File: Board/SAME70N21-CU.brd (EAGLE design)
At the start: 53.3 x 40.3 mm, 35 parts, among them U1 ATSAME70N21A-ANTQFP100_14X14M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

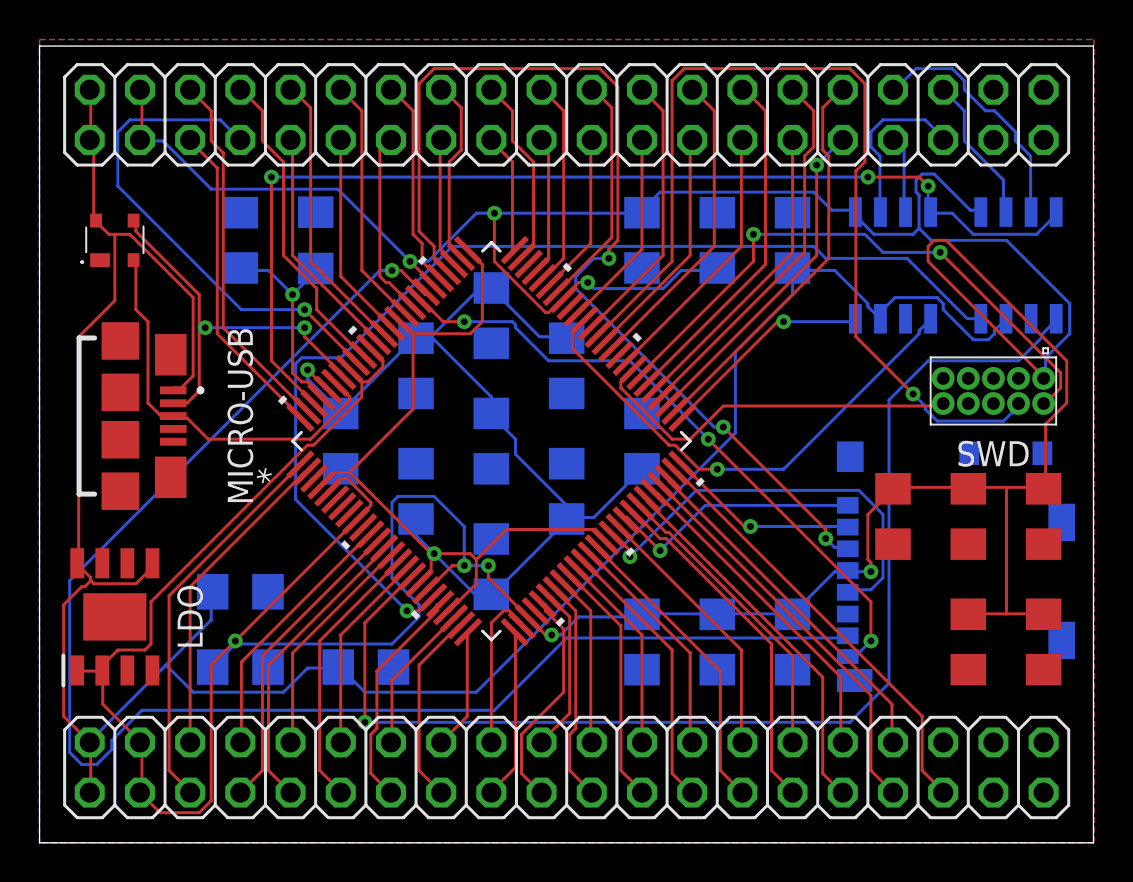
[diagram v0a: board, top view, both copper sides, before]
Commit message: Major revision to first board pcb
- reduced board size
- fixed airwires
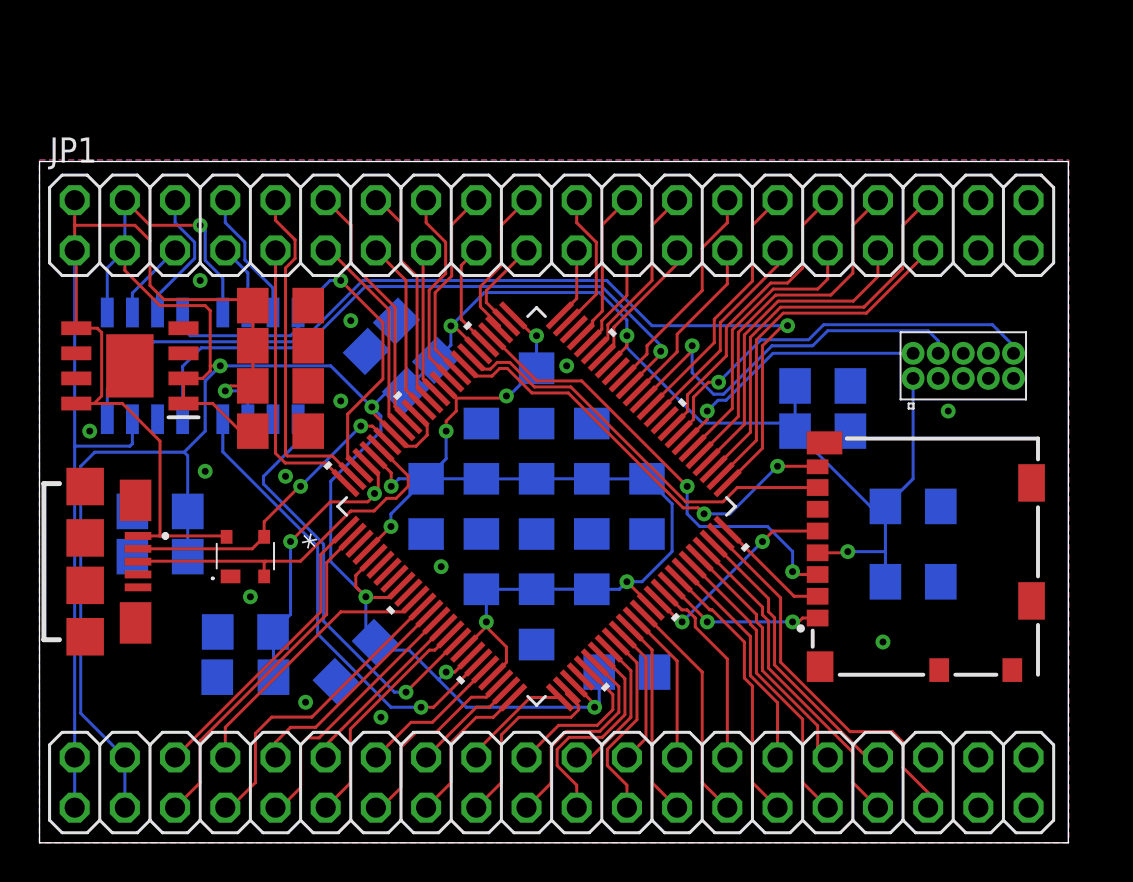
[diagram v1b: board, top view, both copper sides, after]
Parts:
- removed JP3: (no value), pinhead:2X20
- added JP1: (no value), pinhead:2X20
- moved C1 44.9 mm to (6.10, 14.5), flipped to the bottom, turned to 0 degrees
- moved C20 40.9 mm to (6.10, 16.8), flipped to the bottom, turned to 0 degrees
- moved CAN0 38.7 mm to (11.2, 24.1)
- moved CAN1 38.2 mm to (5.33, 24.1)
- moved C2 31.0 mm to (16.0, 9.14), flipped to the bottom, turned to 315 degrees
- moved C21 26.5 mm to (12.2, 25.1), flipped to the top, turned to 0 degrees
- moved C6 24.4 mm to (19.1, 25.4), turned to 45 degrees
- moved C3 22.5 mm to (29.7, 8.64), flipped to the bottom, turned to 180 degrees
- moved R1 22.4 mm to (10.4, 8.38), turned to 180 degrees
- moved C19 19.8 mm to (10.4, 10.7), turned to 0 degrees
- moved C8 18.9 mm to (17.5, 23.9), turned to 45 degrees
- moved ESD 17.3 mm to (10.4, 14.5)
- moved C22 14.9 mm to (12.2, 23.1), flipped to the top, turned to 0 degrees
- moved C23 14.6 mm to (12.2, 27.2), flipped to the top, turned to 0 degrees
- moved C5 13.3 mm to (39.6, 20.8), turned to 180 degrees
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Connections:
- net +3V3: now also JP1.3, JP1.4; no longer JP3.3, JP3.4
- net +5V: now also JP1.1, JP1.2; no longer JP3.1, JP3.2
- net ATSAME70N21_PA0: now also JP1.24; no longer JP3.19
- net ATSAME70N21_PA1: now also JP1.26; no longer JP3.21
- net ATSAME70N21_PA13: now also JP2.17; no longer JP2.18
- net ATSAME70N21_PA16: now also JP2.20; no longer JP2.19
- net ATSAME70N21_PA17: now also JP2.11; no longer JP2.12
- net ATSAME70N21_PA18: now also JP2.12; no longer JP2.11
- net ATSAME70N21_PA19: now also JP2.9; no longer JP2.10
- net ATSAME70N21_PA2: now also JP1.28; no longer JP3.23
- net ATSAME70N21_PA20: now also JP2.10; no longer JP2.9
- net ATSAME70N21_PA21: now also JP2.14; no longer JP2.13
- net ATSAME70N21_PA22: now also JP2.18; no longer JP2.17
- net ATSAME70N21_PA23: now also JP2.19; no longer JP2.20
- net ATSAME70N21_PA3: now also JP1.27; no longer JP3.24
- net ATSAME70N21_PA4: now also JP1.34; no longer JP3.29
- net ATSAME70N21_PA5: now also JP1.35; no longer JP3.32
- net ATSAME70N21_PA7: now also JP2.16; no longer JP2.15
- net ATSAME70N21_PA8: now also JP2.15; no longer JP2.16
- net ATSAME70N21_PA9: now also JP1.33; no longer JP3.30
- net ATSAME70N21_PB12: now also JP1.29; no longer JP3.26
- net ATSAME70N21_PB13: now also JP1.9; no longer JP3.5
- net ATSAME70N21_PB4: now also JP1.22; no longer JP3.18
- net ATSAME70N21_PB5: now also JP1.19; no longer JP3.16
- net ATSAME70N21_PB9: now also JP1.10; no longer JP3.6
- net ATSAME70N21_PD0: now also JP2.6; no longer JP2.5
- net ATSAME70N21_PD1: now also JP1.11; no longer JP3.7
- net ATSAME70N21_PD10: now also JP1.23; no longer JP3.20
- net ATSAME70N21_PD11: now also JP1.25; no longer JP3.22
- net ATSAME70N21_PD13: now also JP1.30; no longer JP3.25
- net ATSAME70N21_PD14: now also JP1.32; no longer JP3.27
- net ATSAME70N21_PD15: now also JP1.21; no longer JP3.17
- net ATSAME70N21_PD16: now also JP1.31; no longer JP3.28
- net ATSAME70N21_PD17: now also JP1.36; no longer JP3.31
- net ATSAME70N21_PD2: now also JP1.12; no longer JP3.8
- net ATSAME70N21_PD3: now also JP1.13; no longer JP3.9
- net ATSAME70N21_PD30: now also JP2.13; no longer JP2.14
- net ATSAME70N21_PD31: now also JP2.5; no longer JP2.6
- net ATSAME70N21_PD4: now also JP1.14; no longer JP3.10
- net ATSAME70N21_PD5: now also JP1.15; no longer JP3.11
- net ATSAME70N21_PD6: now also JP1.16; no longer JP3.12
- net ATSAME70N21_PD7: now also JP1.18; no longer JP3.13
- net ATSAME70N21_PD8: now also JP1.17; no longer JP3.14
- net ATSAME70N21_PD9: now also JP1.20; no longer JP3.15
- net CAN0H: now also JP1.8; no longer JP3.34
- net CAN0L: now also JP1.7; no longer JP3.36
- net CAN1H: now also JP1.6; no longer JP3.33
- net CAN1L: now also JP1.5; no longer JP3.35
- net GND: now also JP1.37, JP1.38, JP1.39, JP1.40; no longer JP3.37, JP3.38, JP3.39, JP3.40
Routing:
- net +3V3: track 243.3 -> 171.3 mm, vias 8 -> 9
- net MSD-DAT0: track 76.4 -> 21.1 mm, vias 1 -> 0
- net +5V: track 122.9 -> 79.3 mm, vias 0 -> 1
- net CAN0TX: track 60.3 -> 21.5 mm
- net CAN1RX: track 10.8 -> 48.6 mm
- net CAN-STBY: track 54.6 -> 22.0 mm, vias 3 -> 1
- net CAN0RX: track 55.1 -> 23.5 mm
- net VCCINT: track 88.1 -> 56.8 mm, vias 2 -> 7
- net MSD-CMD: track 51.9 -> 22.9 mm, vias 3 -> 2
- net SWCLK: track 48.2 -> 20.2 mm
- net SWDIO: track 29.9 -> 13.6 mm, vias 2 -> 1
- net ATSAME70N21_PD1: track 25.4 -> 10.6 mm, vias 1 -> 0
- net MSD-CLK: track 21.5 -> 10.5 mm, vias 1 -> 2
- net MSD-DAT1: track 32.8 -> 22.4 mm, vias 3 -> 2
- net CAN1TX: track 25.6 -> 32.4 mm
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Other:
- board size 53.3 x 40.3 mm -> 52 x 34.5 mm

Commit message: SAME70N21-CU Board V1
Fixed SD Card Slot orientation
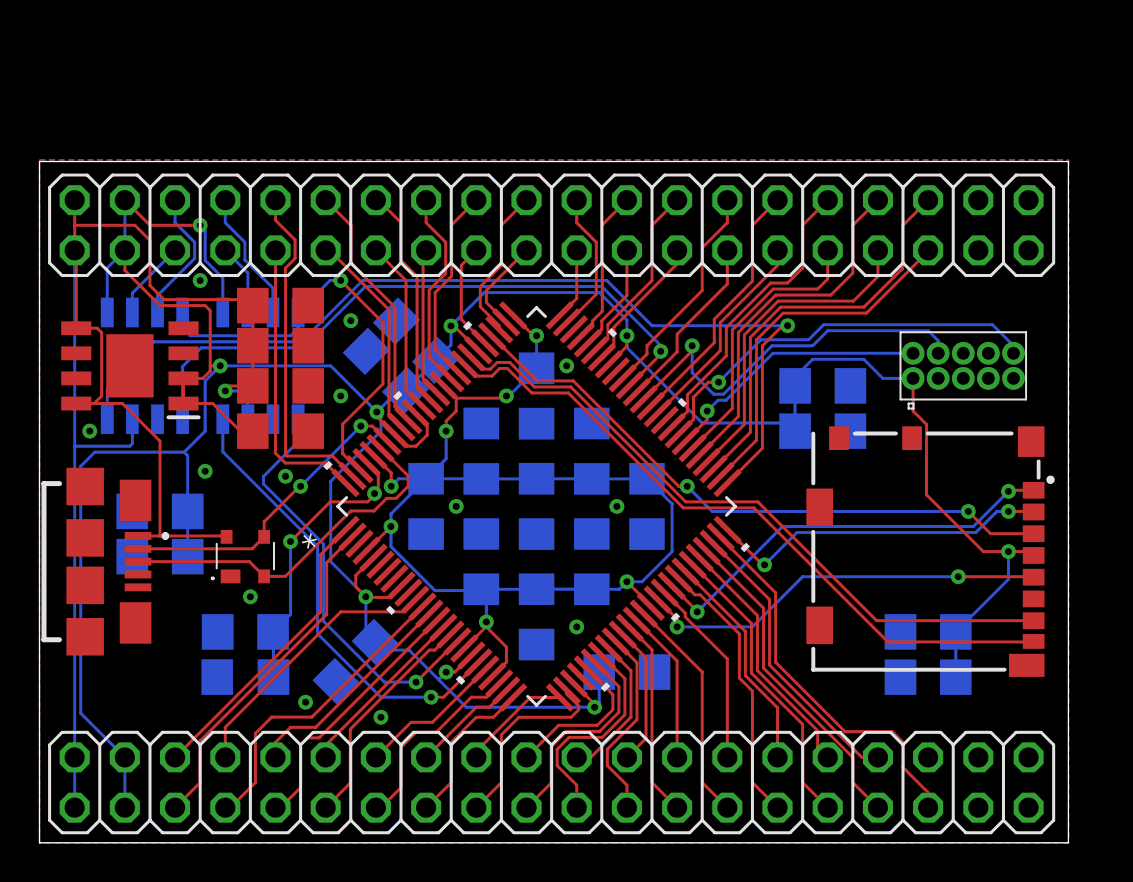
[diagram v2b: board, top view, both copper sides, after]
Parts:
- moved MICRO-SD 11.4 mm to (50.5, 14.7), turned to 90 degrees
- moved C9 8.67 mm to (45.0, 8.38), turned to 0 degrees
- moved C7 2.65 mm to (45.0, 10.7), turned to 0 degrees
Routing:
- net MSD-DAT2: track 8.24 -> 21.4 mm
- net MSD-DAT0: track 21.1 -> 34.3 mm
- net MSD-DAT1: track 22.4 -> 35.0 mm, vias 2 -> 0
- net MSD-DAT3: track 5.95 -> 17.3 mm, vias 0 -> 2
- net MSD-CLK: track 10.5 -> 20.9 mm
- net MSD-CMD: track 22.9 -> 31.5 mm
- net VCCINT: track 56.8 -> 63.3 mm
- net +3V3: track 171.3 -> 177.9 mm
